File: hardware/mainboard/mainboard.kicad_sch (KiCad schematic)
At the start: 0 parts

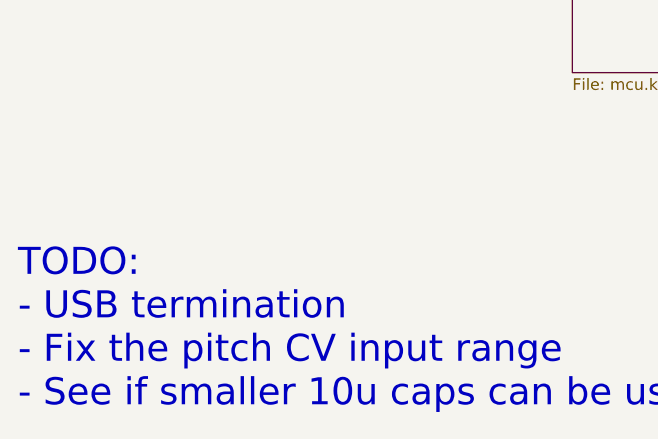
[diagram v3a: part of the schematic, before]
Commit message: Normalize component values
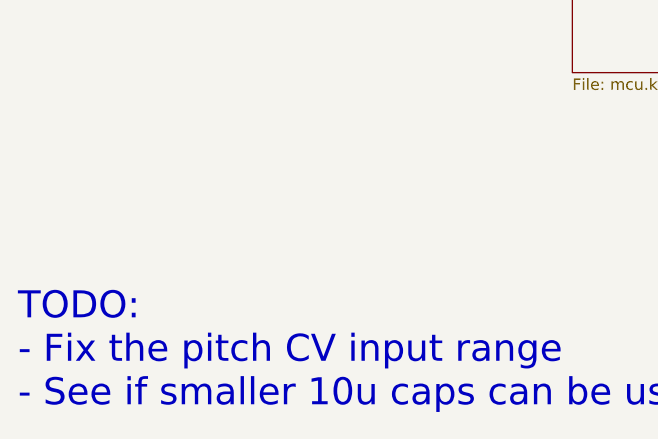
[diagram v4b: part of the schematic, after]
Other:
- note added: "TODO: - Fix the pitch CV input range - See if smaller 10u caps can be used in the output amps"
- note removed: "TODO: - USB termination - Fix the pitch CV input range - See if smaller 10u caps can be used in the output amps"

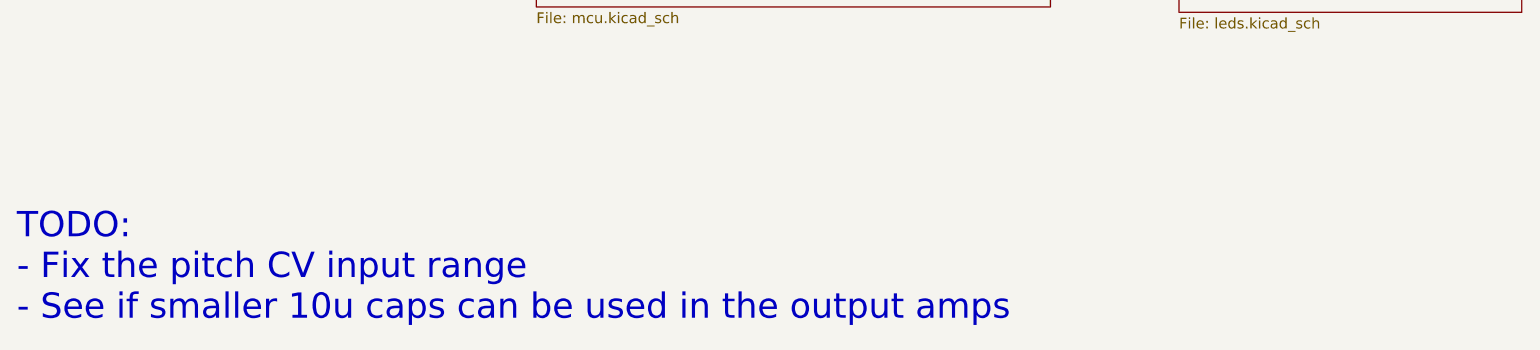
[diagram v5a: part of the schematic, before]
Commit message: Audit BOM, replace some parts with alts
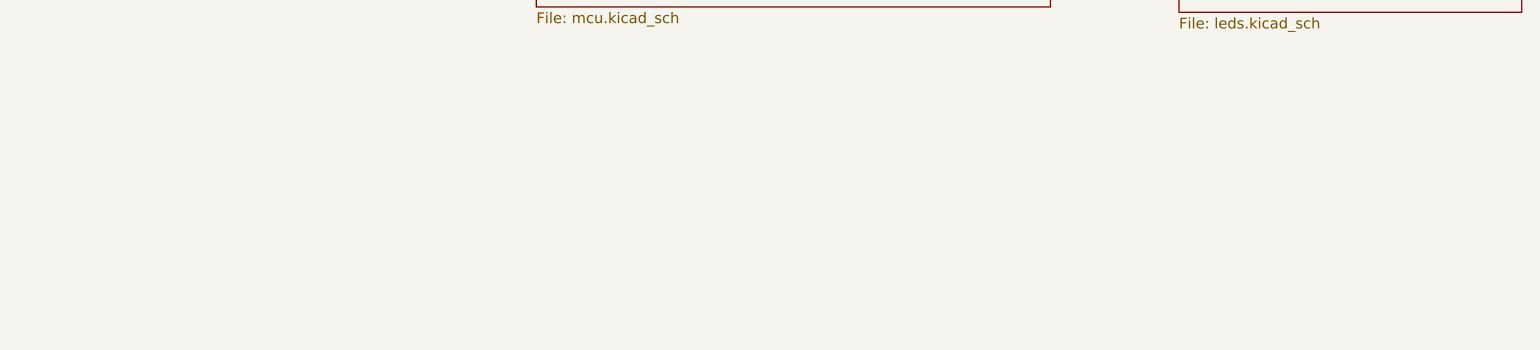
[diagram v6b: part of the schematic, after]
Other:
- note removed: "TODO: - Fix the pitch CV input range - See if smaller 10u caps can be used in the output amps"
